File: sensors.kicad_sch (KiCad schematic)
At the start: 0 parts

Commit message: Schematic done (for now), WIP on layout
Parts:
- added C17, C18, C19: 0.1uF/50V, Capacitor_SMD:C_0603_1608Metric_Pad1.08x0.95mm_HandSolder, symbol Device:C_Small
- added Q8: MMBT2369LT1G, Package_TO_SOT_SMD:SOT-23_Handsoldering, symbol Device:Q_NPN_BEC
- added R34: 51k, Resistor_SMD:R_0603_1608Metric_Pad0.98x0.95mm_HandSolder, symbol Device:R
- added R35: 100k, Resistor_SMD:R_0603_1608Metric_Pad0.98x0.95mm_HandSolder, symbol Device:R
- added RV1: PTN10-D10SB20, Resistors_custom:TRIM_PTN10-D10SB20, symbol Device:R_Potentiometer
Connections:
- new net: Q8.3 (C), R34.1, RV1.3
- new net: Q8.1 (B), R35.2
- new net +3V3: RV1.2
- new net GND: C17.2, C18.2, C19.2, Q8.2 (E)
- new net LIGHTSEN_SIG: C18.1, R35.1
- new net LIGHT_SENSOR: C17.1, R34.2
- new net RESET_LEVER: C19.1
- no-connect marks 0 -> 1
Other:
- note added: "Light sensor"
- note added: "Reset lever"

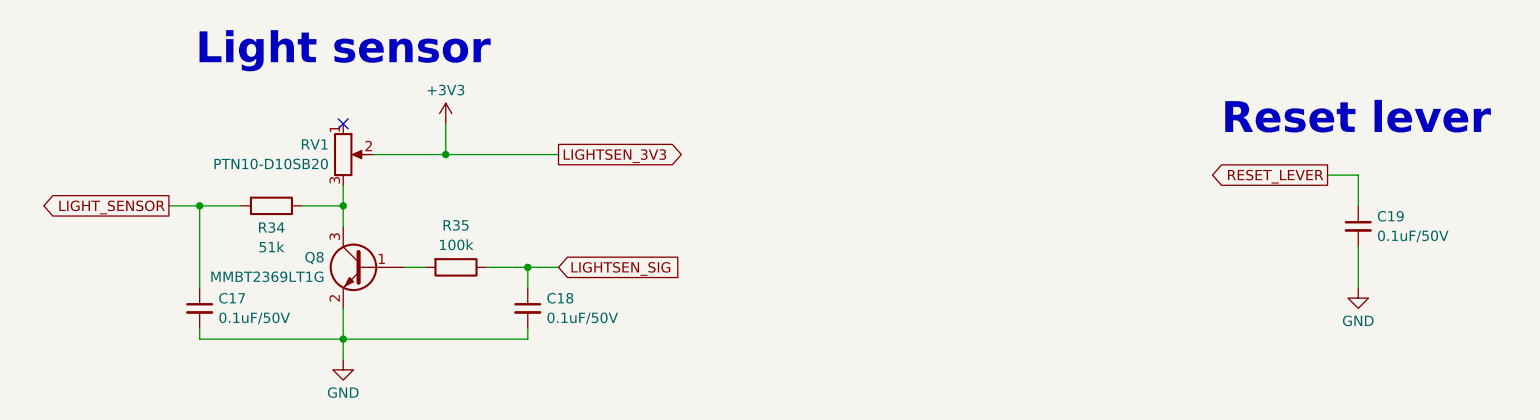
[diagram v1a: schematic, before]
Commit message: Routing done, need to work on silkscreen
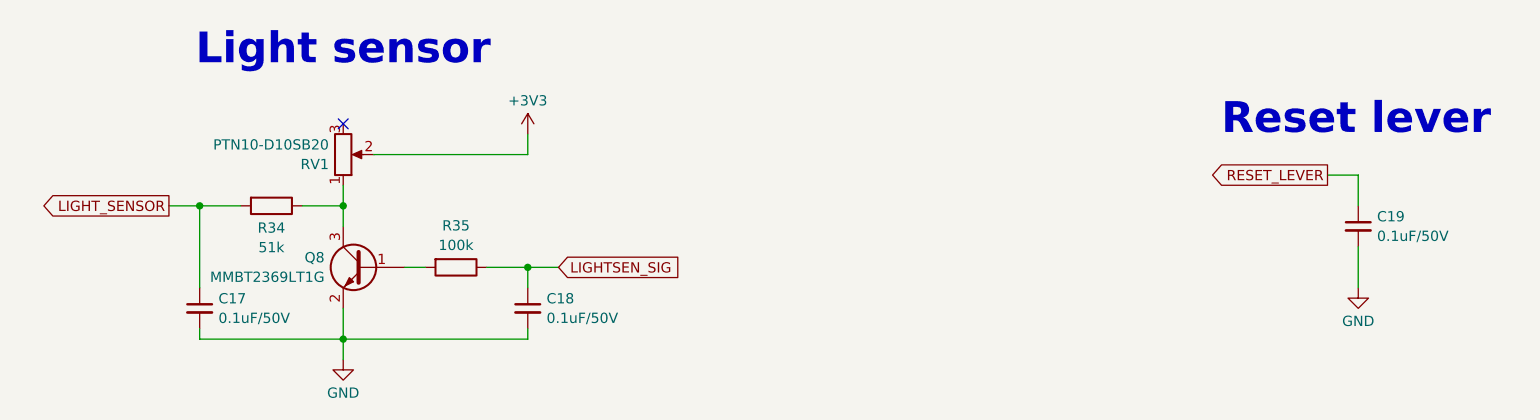
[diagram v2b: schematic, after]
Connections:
- net at Q8.3 (C), R34.1: now also RV1.1; no longer RV1.3
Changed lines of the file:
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@@
-		(color 0 0 0 0)
-	)
-	(junction
-		(at 93.98 83.82)
-		(diameter 0)
 		(color 0 0 0 0)
 	)
@@
 	(wire
 		(pts
-			(xy 93.98 83.82) (xy 93.98 80.01)
+			(xy 104.14 83.82) (xy 104.14 81.28)
 		)
 		(stroke
@@
 	(wire
 		(pts
-			(xy 93.98 83.82) (xy 107.95 83.82)
-		)
-		(stroke
-			(width 0)
-			(type default)
-		)
-	)
-	(wire
-		(pts
 			(xy 104.14 106.68) (xy 81.28 106.68)
 		)
@@
 	(wire
 		(pts
-			(xy 85.09 83.82) (xy 93.98 83.82)
+			(xy 85.09 83.82) (xy 104.14 83.82)
 		)
 		(stroke
@@
 		)
 	)
-	(global_label "LIGHTSEN_3V3"
-		(shape output)
-		(at 107.95 83.82 0)
+	(global_label "LIGHTSEN_SIG"
+		(shape input)
+		(at 107.95 97.79 0)
 		(fields_autoplaced yes)
 		(effects
@@
 		)
 		(property "Intersheetrefs" "${INTERSHEET_REFS}"
-			(at 124.3004 83.82 0)
-			(effects
-				(font
-					(size 1.27 1.27)
-				)
-				(justify left)
-				(hide yes)
-			)
-		)
-	)
-	(global_label "LIGHTSEN_SIG"
-		(shape input)
-		(at 107.95 97.79 0)
-		(fields_autoplaced yes)
-		(effects
-			(font
-				(size 1.27 1.27)
-			)
-			(justify left)
-		)
-		(property "Intersheetrefs" "${INTERSHEET_REFS}"
 			(at 123.8771 97.79 0)
 			(effects
@@
 	(symbol
 		(lib_id "power:+3V3")
-		(at 93.98 80.01 0)
+		(at 104.14 81.28 0)
 		(unit 1)
 		(exclude_from_sim no)
@@
 		(fields_autoplaced yes)
 		(property "Reference" "#PWR033"
-			(at 93.98 83.82 0)
+			(at 104.14 85.09 0)
 			(effects
 				(font
@@
 		)
 		(property "Value" "+3V3"
-			(at 93.98 75.8769 0)
+			(at 104.14 77.1469 0)
 			(effects
 				(font
@@
 		)
 		(property "Footprint" ""
-			(at 93.98 80.01 0)
+			(at 104.14 81.28 0)
 			(effects
 				(font
@@
 		)
 		(property "Datasheet" ""
-			(at 93.98 80.01 0)
+			(at 104.14 81.28 0)
 			(effects
 				(font
@@
 		)
 		(property "Description" "Power symbol creates a global label with name \"+3V3\""
-			(at 93.98 80.01 0)
+			(at 104.14 81.28 0)
 			(effects
 				(font
@@
 		(lib_id "Device:R_Potentiometer")
 		(at 81.28 83.82 0)
+		(mirror x)
 		(unit 1)
 		(exclude_from_sim no)
@@
 		(on_board yes)
 		(dnp no)
-		(fields_autoplaced yes)
 		(property "Reference" "RV1"
-			(at 79.502 82.6078 0)
+			(at 79.502 85.0322 0)
 			(effects
 				(font
@@
 		)
 		(property "Value" "PTN10-D10SB20"
-			(at 79.502 85.0321 0)
-			(effects
-				(font
+			(at 79.502 82.6079 0)
+			(effects
+				(font
